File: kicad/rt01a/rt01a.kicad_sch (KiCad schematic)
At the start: 24 parts, among them J1 Barrel_Jack_Switch, J2 USB_C_Receptacle_USB2.0_14P, Q1 DMP3099L, U1 R-78E5.0-1.0, U2 MCP73831-2-OT, U3 TLV75533PDBV, U4 MCP111T-xxxE_TT

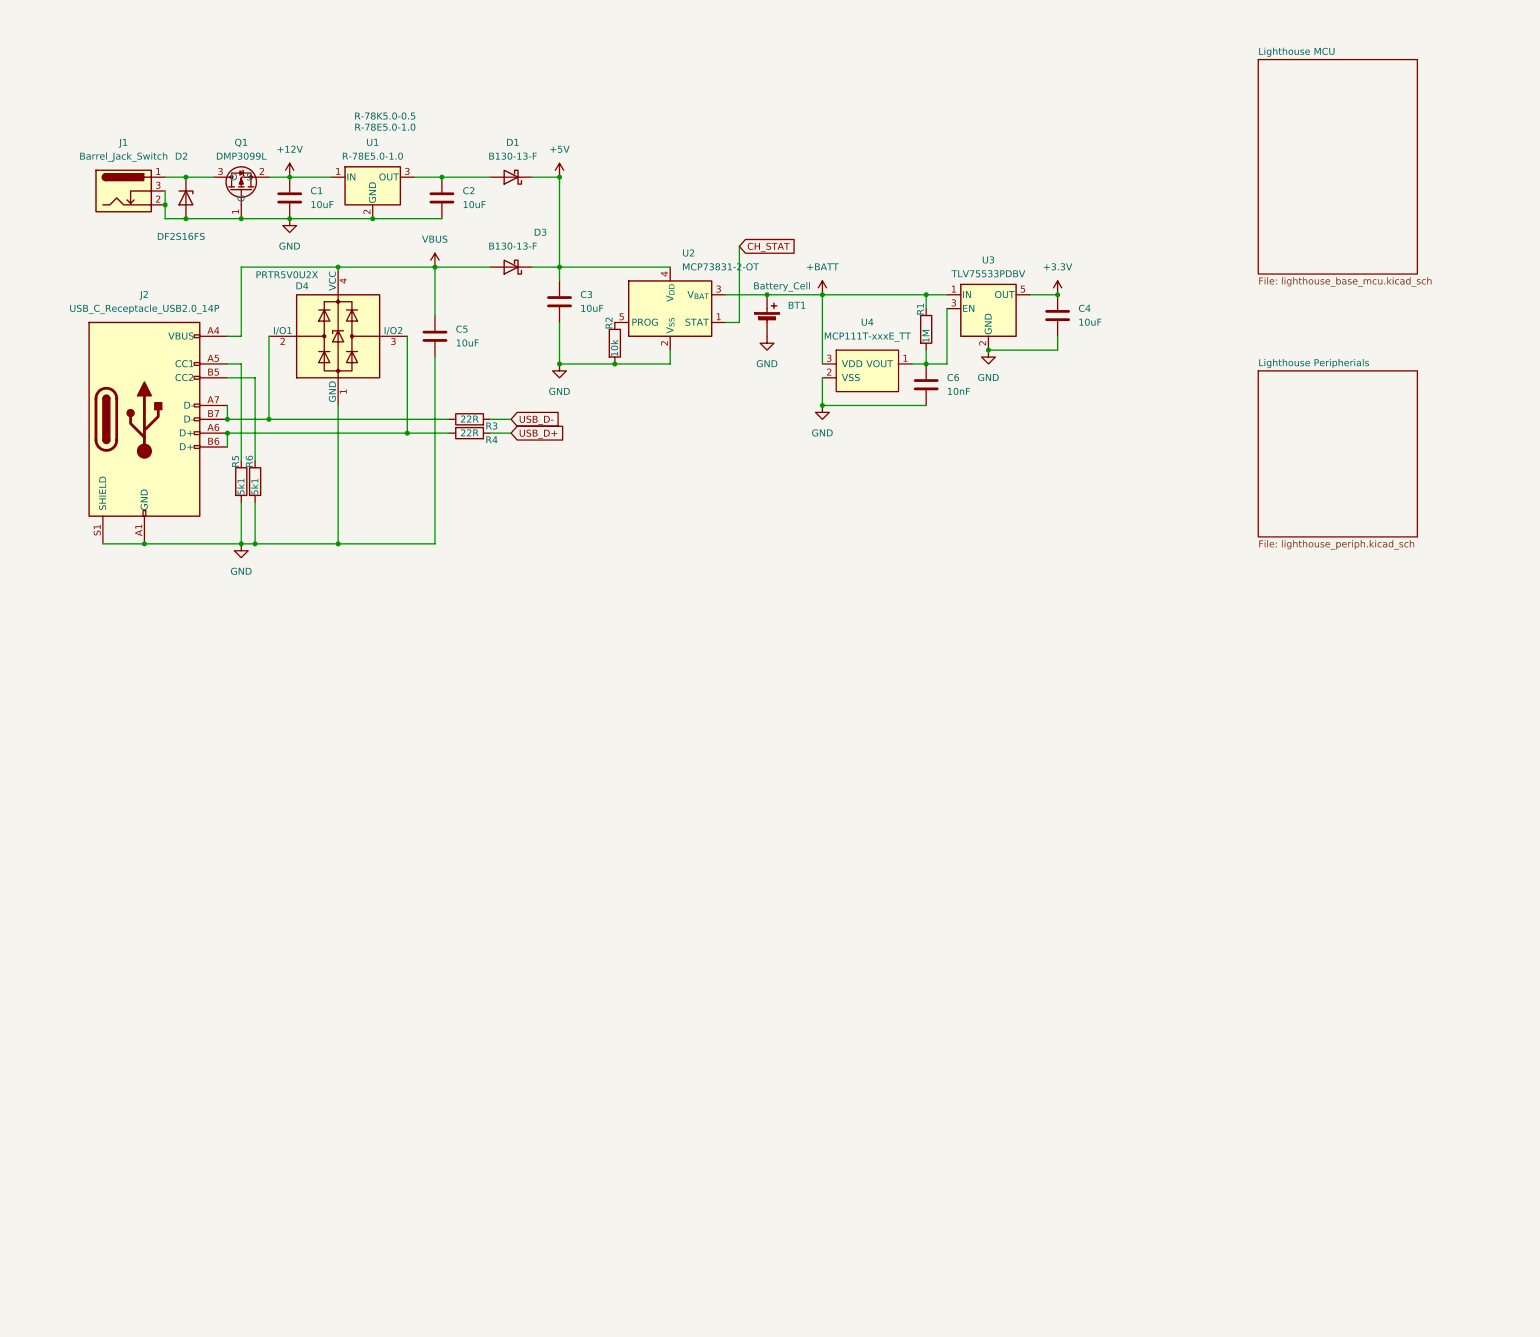
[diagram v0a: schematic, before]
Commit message: removed rt01a_1, _2, not needed anymore
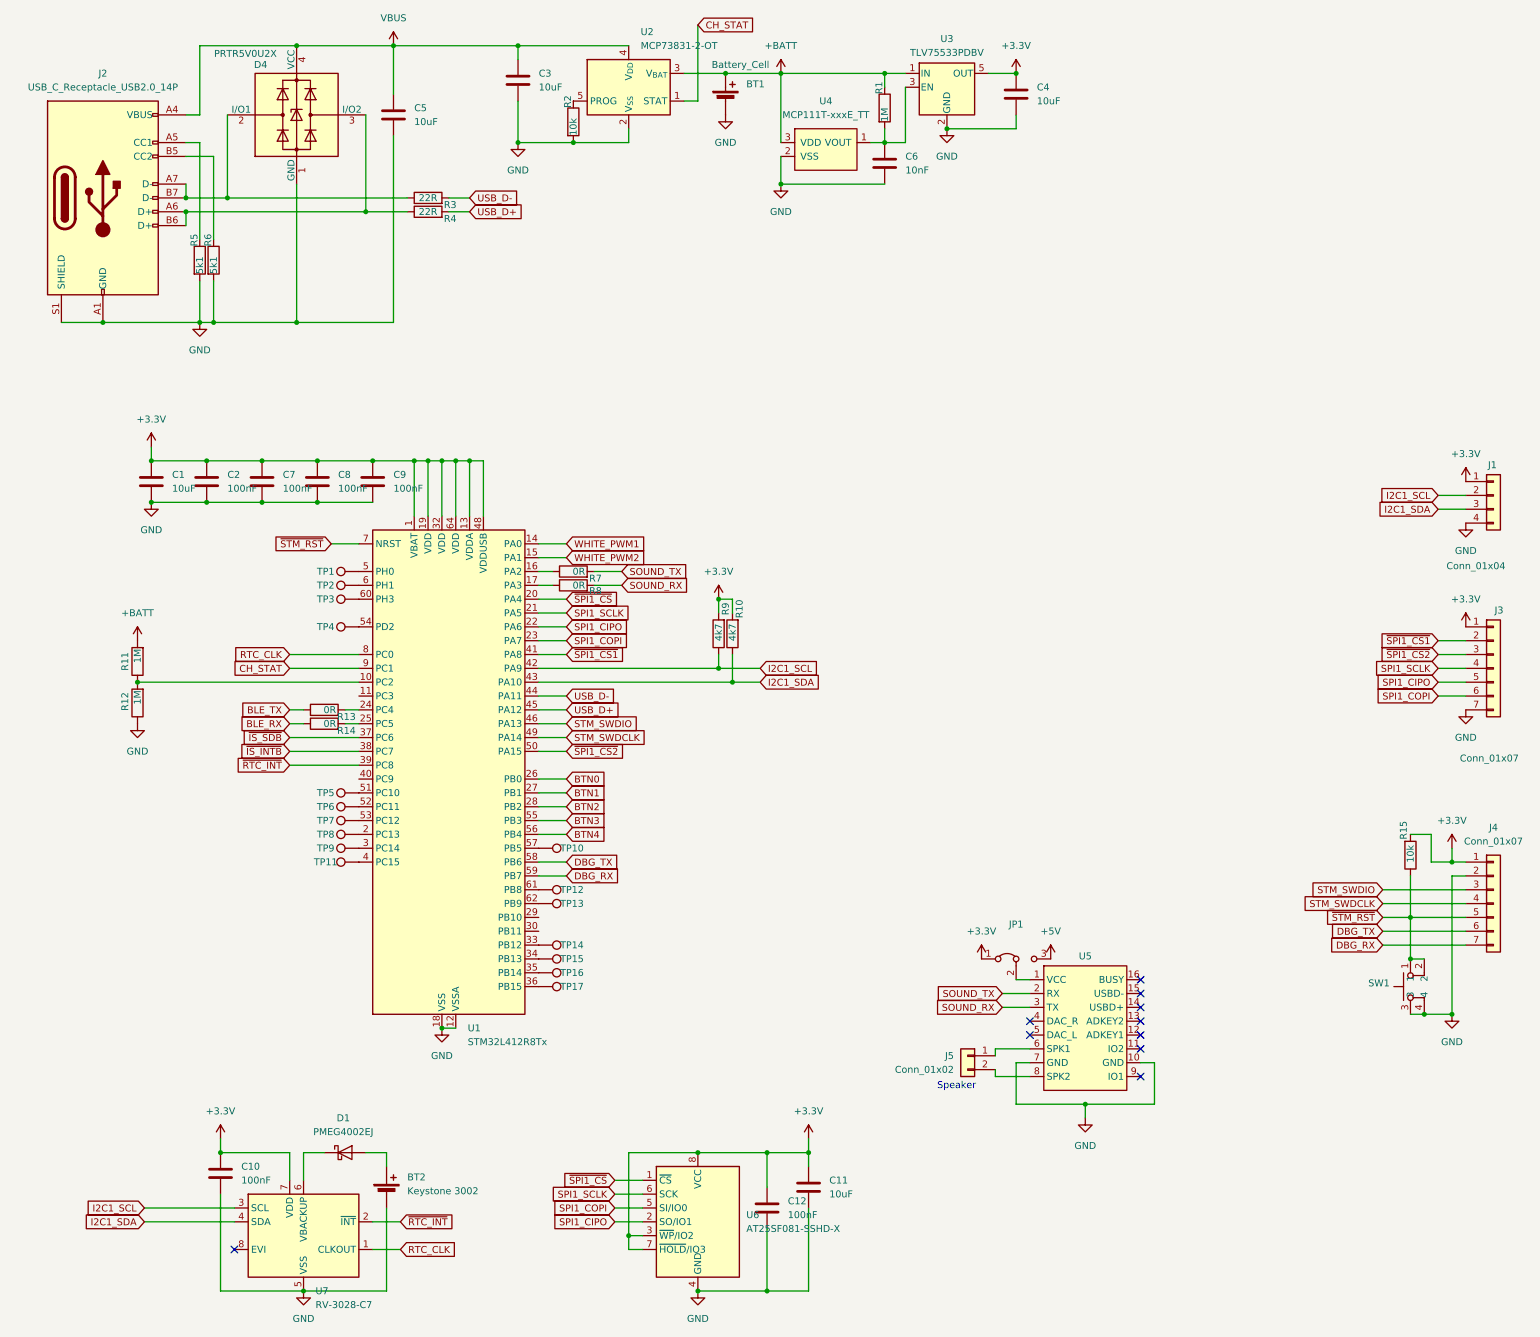
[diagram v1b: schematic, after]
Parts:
- removed D1, D3: B130-13-F, Diode_SMD:D_SMA_Handsoldering, symbol Device:D_Schottky
- removed D2: DF2S16FS, Diode_SMD:D_SOD-523, symbol Diode:ESD5Zxx
- removed J1: Barrel_Jack_Switch, Connector_BarrelJack:BarrelJack_CUI_PJ-063AH_Horizontal, symbol Connector:Barrel_Jack_Switch
- removed Q1: DMP3099L, Package_TO_SOT_SMD:SOT-23-3, symbol lighthouse1:DMP3099L_PMOSFET
- removed U1: R-78E5.0-1.0, Converter_DCDC:Converter_DCDC_RECOM_R-78E-0.5_THT, symbol Regulator_Switching:R-78E5.0-1.0
- added BT2: Keystone 3002, Battery:BatteryHolder_Keystone_3002_1x2032, symbol Device:Battery_Cell
- added C10, C12, C7, C8, C9: 100nF, Capacitor_SMD:C_0603_1608Metric_Pad1.08x0.95mm_HandSolder, symbol Device:C
- added C11: 10uF, Capacitor_SMD:C_0805_2012Metric_Pad1.18x1.45mm_HandSolder, symbol Device:C
- added D1: PMEG4002EJ, Diode_SMD:D_SOD-323F, symbol Diode:PMEG4002EJ
- added J1: Conn_01x04, Connector_PinHeader_2.54mm:PinHeader_1x04_P2.54mm_Vertical, symbol Connector_Generic:Conn_01x04
- added J3: Conn_01x07, Connector_PinHeader_2.54mm:PinHeader_1x07_P2.54mm_Vertical, symbol Connector_Generic:Conn_01x07
- added J4: Conn_01x07, Connector_PinHeader_1.27mm:PinHeader_1x07_P1.27mm_Vertical, symbol Connector_Generic:Conn_01x07
- added J5: Conn_01x02, Connector_PinHeader_2.54mm:PinHeader_1x02_P2.54mm_Vertical, symbol Connector_Generic:Conn_01x02
- added JP1: Jumper_3_Bridged12, Jumper:SolderJumper-3_P1.3mm_Bridged2Bar12_RoundedPad1.0x1.5mm, symbol Jumper:Jumper_3_Bridged12
- added R10, R9: 4k7, Resistor_SMD:R_0603_1608Metric_Pad0.98x0.95mm_HandSolder, symbol Device:R
- added R11, R12: 1M, Resistor_SMD:R_0603_1608Metric_Pad0.98x0.95mm_HandSolder, symbol Device:R
- added R13, R14, R7, R8: 0R, Resistor_SMD:R_0603_1608Metric_Pad0.98x0.95mm_HandSolder, symbol Device:R
- added R15: 10k, Resistor_SMD:R_0603_1608Metric_Pad0.98x0.95mm_HandSolder, symbol Device:R
- added SW1: ~, lighthouse:PTS526, symbol lighthouse1:SW_PTS5236
- added TP1, TP10, TP11, TP12, TP13, TP14, TP15, TP16, TP17, TP2, TP3, TP4, TP5, TP6, TP7, TP8, TP9: TestPoint, TestPoint:TestPoint_Pad_D1.0mm, symbol Connector:TestPoint
- added U1: STM32L412R8Tx, Package_QFP:LQFP-64_10x10mm_P0.5mm, symbol MCU_ST_STM32L4:STM32L412R8Tx
- added U5: ~, lighthouse:DFPlayer_Mini-TF-16P, symbol lighthouse1:DFPlayer_Mini
- added U6: AT25SF081-SSHD-X, Package_SO:SOIC-8_3.9x4.9mm_P1.27mm, symbol Memory_Flash:AT25SF081-SSHD-X
- added U7: RV-3028-C7, Package_SON:MicroCrystal_C7_SON-8_1.5x3.2mm_P0.9mm, symbol Timer_RTC:RV-3028-C7
- C2: value 10uF -> 100nF; footprint Capacitor_SMD:C_0805_2012Metric_Pad1.18x1.45mm_HandSolder -> Capacitor_SMD:C_0603_1608Metric_Pad1.08x0.95mm_HandSolder
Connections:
- net +12V is gone; now on net +3.3V: C1.1
- net +3.3V: now also C2.1, C10.1, C11.1, C12.1, C7.1, C8.1, C9.1, J1.1 (Pin_1), J3.1 (Pin_1), J4.1 (Pin_1), JP1.1 (A), R10.2, R15.2, R9.2, U1.1 (VBAT), U1.13 (VDDA), U1.19 (VDD), U1.32 (VDD), U1.48 (VDDUSB), U1.64 (VDD), U6.3 (~{WP}/IO2), U6.7 (~{HOLD}/IO3), U6.8 (VCC), U7.7 (VDD)
- net +5V: now also JP1.3 (B); no longer C3.1, U2.4 (V_{DD})
- net +BATT: now also R11.2
- net CH_STAT: now also U1.9 (PC1)
- net GND: now also BT2.2 (-), C10.2, C11.2, C12.2, C7.2, C8.2, C9.2, J1.4 (Pin_4), J3.7 (Pin_7), J4.2 (Pin_2), R12.1, SW1.3, SW1.4, U1.12 (VSSA), U1.18 (VSS), U1.31 (VSS), U1.47 (VSS), U1.63 (VSS), U5.10 (GND), U5.7 (GND), U6.4 (GND), U7.5 (VSS)
- net USB_D+: now also U1.45 (PA12)
- net USB_D-: now also U1.44 (PA11)
- net VBUS: now also C3.1, U2.4 (V_{DD})
- new net: JP1.2 (C), U5.1 (VCC)
- new net: TP11.1, U1.4 (PC15)
- new net: TP15.1, U1.34 (PB13)
- new net: TP10.1, U1.57 (PB5)
- new net: R13.2, U1.24 (PC4)
- new net: TP5.1, U1.51 (PC10)
- new net: TP2.1, U1.6 (PH1)
- new net: J5.1 (Pin_1), U5.6 (SPK1)
- new net: J5.2 (Pin_2), U5.8 (SPK2)
- new net: TP4.1, U1.54 (PD2)
- new net: TP13.1, U1.62 (PB9)
- new net: TP9.1, U1.3 (PC14)
- new net: TP16.1, U1.35 (PB14)
- new net: TP7.1, U1.53 (PC12)
- new net: D1.1 (K), U7.6 (VBACKUP)
- new net: BT2.1 (+), D1.2 (A)
- new net: R11.1, R12.2, U1.10 (PC2)
- new net: R14.2, U1.25 (PC5)
- new net: R8.1, U1.17 (PA3)
- new net: TP3.1, U1.60 (PH3)
- new net: TP17.1, U1.36 (PB15)
- new net: TP14.1, U1.33 (PB12)
- new net: R7.1, U1.16 (PA2)
- new net: TP8.1, U1.2 (PC13)
- new net: TP1.1, U1.5 (PH0)
- new net: TP6.1, U1.52 (PC11)
- new net: TP12.1, U1.61 (PB8)
- new net BLE_RX: R14.1
- new net BLE_TX: R13.1
- new net BTN0: U1.26 (PB0)
- new net BTN1: U1.27 (PB1)
- new net BTN2: U1.28 (PB2)
- new net BTN3: U1.55 (PB3)
- new net BTN4: U1.56 (PB4)
- new net DBG_RX: J4.7 (Pin_7), U1.59 (PB7)
- new net DBG_TX: J4.6 (Pin_6), U1.58 (PB6)
- new net I2C1_SCL: J1.2 (Pin_2), R9.1, U1.42 (PA9), U7.3 (SCL)
- new net I2C1_SDA: J1.3 (Pin_3), R10.1, U1.43 (PA10), U7.4 (SDA)
- new net RTC_CLK: U1.8 (PC0), U7.1 (CLKOUT)
- new net SOUND_RX: R8.2, U5.3 (TX)
- new net SOUND_TX: R7.2, U5.2 (RX)
- new net SPI1_CIPO: J3.5 (Pin_5), U1.22 (PA6), U6.2 (SO/IO1)
- new net SPI1_COPI: J3.6 (Pin_6), U1.23 (PA7), U6.5 (SI/IO0)
- new net SPI1_SCLK: J3.4 (Pin_4), U1.21 (PA5), U6.6 (SCK)
- new net STM_SWDCLK: J4.4 (Pin_4), U1.49 (PA14)
- new net STM_SWDIO: J4.3 (Pin_3), U1.46 (PA13)
- new net WHITE_PWM1: U1.14 (PA0)
- new net WHITE_PWM2: U1.15 (PA1)
- new net ~{IS_INTB}: U1.38 (PC7)
- new net ~{IS_SDB}: U1.37 (PC6)
- new net ~{RTC_INT}: U1.39 (PC8), U7.2 (~{INT})
- new net ~{SPI1_CS1}: J3.2 (Pin_2), U1.41 (PA8)
- new net ~{SPI1_CS2}: J3.3 (Pin_3), U1.50 (PA15)
- new net ~{SPI1_CS}: U1.20 (PA4), U6.1 (~{CS})
- new net ~{STM_RST}: J4.5 (Pin_5), R15.1, SW1.1, SW1.2, U1.7 (NRST)
- no-connect marks 0 -> 10
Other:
- removed sheet Lighthouse MCU
- removed sheet Lighthouse Peripherials
- note added: "Speaker"
- note removed: "R-78K5.0-0.5 R-78E5.0-1.0"
- title: (none) -> round timer 1
- moved on the sheet: BT1, C3, C4, C5, C6, D4, J2, R1, R2, R3, R4, R5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

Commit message: rt01a added footprint, some placements done
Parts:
- removed BT2: Keystone 3002, Battery:BatteryHolder_Keystone_3002_1x2032, symbol Device:Battery_Cell
- removed D1: PMEG4002EJ, Diode_SMD:D_SOD-323F, symbol Diode:PMEG4002EJ
- removed J1: Conn_01x04, Connector_PinHeader_2.54mm:PinHeader_1x04_P2.54mm_Vertical, symbol Connector_Generic:Conn_01x04
- removed J3: Conn_01x07, Connector_PinHeader_2.54mm:PinHeader_1x07_P2.54mm_Vertical, symbol Connector_Generic:Conn_01x07
- added R16: 10k, Resistor_SMD:R_0603_1608Metric_Pad0.98x0.95mm_HandSolder, symbol Device:R
- added TP18, TP19, TP20, TP21: TestPoint, TestPoint:TestPoint_Pad_D1.0mm, symbol Connector:TestPoint
- C3: value 10uF -> 10nF; footprint Capacitor_SMD:C_0805_2012Metric_Pad1.18x1.45mm_HandSolder -> Capacitor_SMD:C_0603_1608Metric_Pad1.08x0.95mm_HandSolder
- SW1: value ~ -> EVPBT3G4A000; footprint lighthouse:PTS526 -> rt:EVPBT3
- U5: footprint lighthouse:DFPlayer_Mini-TF-16P -> rt:DFPlayer_Mini-TF-16P
- renumbered C5 to C1, C4 to C2, C6 to C4, C1 to C5, C2 to C6, D4 to D1, J2 to J1, U2 to U1, U3 to U2, U4 to U3, U1 to U4
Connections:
- net +3.3V: now also TP18.1
- net GND: now also R16.1, TP21.1
- net I2C1_SCL: now also TP19.1
- net I2C1_SDA: now also TP20.1
- net VBUS: no longer C3.1
- net ~{STM_RST}: now also C3.1
- net at U7.6 (VBACKUP): now also R16.2
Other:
- moved on the sheet: BT1, C1, C2, C4, D1, J1, R1, R2, R3, R4, R5, R6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

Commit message: schematics seems done
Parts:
- removed J5: Conn_01x02, Connector_PinHeader_2.54mm:PinHeader_1x02_P2.54mm_Vertical, symbol Connector_Generic:Conn_01x02
- removed JP1: Jumper_3_Bridged12, Jumper:SolderJumper-3_P1.3mm_Bridged2Bar12_RoundedPad1.0x1.5mm, symbol Jumper:Jumper_3_Bridged12
- removed R13: 0R, Resistor_SMD:R_0603_1608Metric_Pad0.98x0.95mm_HandSolder, symbol Device:R
- removed TP17, TP18, TP19, TP20, TP21: TestPoint, TestPoint:TestPoint_Pad_D1.0mm, symbol Connector:TestPoint
- added C13, C22: 10uF, Capacitor_SMD:C_0805_2012Metric_Pad1.18x1.45mm_HandSolder, symbol Device:C
- added C14, C20, C21, C23: 100nF, Capacitor_SMD:C_0603_1608Metric_Pad1.08x0.95mm_HandSolder, symbol Device:C
- added C15, C16, C17, C18, C19: 10nF, Capacitor_SMD:C_0603_1608Metric_Pad1.08x0.95mm_HandSolder, symbol Device:C
- added D2: D_Schottky, Diode_SMD:D_SOD-523, symbol Device:D_Schottky
- added D3, D4, D5, D6, D7, D8: ESD5Zxx, Diode_SMD:D_SMF, symbol Diode:ESD5Zxx
- added Q1, Q2: Q_NMOS_DGS, Package_TO_SOT_SMD:SOT-23-3, symbol Device:Q_NMOS_DGS
- added R15: 10R, Resistor_SMD:R_0603_1608Metric_Pad0.98x0.95mm_HandSolder, symbol Device:R
- added R17: 1M, Resistor_SMD:R_0603_1608Metric_Pad0.98x0.95mm_HandSolder, symbol Device:R
- added R18, R19, R20, R21, R22, R23, R24, R25, R26, R27, R28, R29: 10k, Resistor_SMD:R_0603_1608Metric_Pad0.98x0.95mm_HandSolder, symbol Device:R
- added U10: LTR-303ALS-01, OptoDevice:Lite-On_LTR-303ALS-01, symbol Sensor_Optical:LTR-303ALS-01
- added U11: LSM303C, Package_LGA:LGA-12_2x2mm_P0.5mm, symbol Sensor_Motion:LSM303C
- added U8: GC9A01, rt:FP-128HR01A, symbol rt:GC9A01
- added U9: SHTC3, Sensor_Humidity:Sensirion_DFN-4-1EP_2x2mm_P1mm_EP0.7x1.6mm, symbol Sensor_Humidity:SHTC3
- R14: value 0R -> 1M
- U7: renamed from U5; footprint rt:DFPlayer_Mini-TF-16P -> rt:DFPlayer_Mini-TF-16P_Minimal; symbol lighthouse1:DFPlayer_Mini -> rt:DFPlayer_Mini_Minimal
- renumbered C5 to C1, C4 to C10, C2 to C11, C3 to C12, C6 to C2, C10 to C3, C7 to C4, C8 to C5, C9 to C6, C1 to C7, C12 to C8, C11 to C9, J4 to J2, R11 to R1, R2 to R10, R9 to R11, R10 to R12, R1 to R13, R15 to R16, R12 to R2, R5 to R3, R6 to R4, R16 to R5, R3 to R6, R4 to R7, R7 to R8, R8 to R9, U7 to U1, U4 to U2, U1 to U3, U6 to U4, U3 to U5, U2 to U6
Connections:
- net BTN4 is gone; now on net BTN3: U2.56 (PB4)
- net WHITE_PWM1 is gone; now on net RTC_CLK: U2.14 (PA0)
- net ~{IS_SDB} is gone; now on net CH_STAT: U2.37 (PC6)
- net +3.3V: now also TP1.1, TP14.1, U7.1 (VCC), C13.1, C14.1, C20.1, C21.1, C22.1, C23.1, D2.1 (K), R23.2, R24.2, R25.2, R26.2, R27.2, U10.1 (VDD), U11.10 (VDDIO), U11.9 (VDD), U8.3 (LEDA), U8.4 (VDD), U9.1 (VDD)
- net BTN1: now also U2.28 (PB2), R20.1; no longer U2.27 (PB1)
- net BTN2: now also U2.55 (PB3), R21.1; no longer U2.28 (PB2)
- net BTN3: now also R22.1; no longer U2.55 (PB3)
- net CH_STAT: no longer U2.9 (PC1)
- net DBG_RX: now also U2.8 (PC0); no longer U2.59 (PB7)
- net DBG_TX: now also U2.9 (PC1); no longer U2.58 (PB6)
- net GND: now also R14.2, TP11.1, TP13.1, TP2.1, TP7.1, TP9.1, C13.2, C14.2, C15.2, C16.2, C17.2, C18.2, C19.2, C20.2, C21.2, C22.2, C23.2, D3.2 (A), D4.2 (A), D5.2 (A), D6.2 (A), D7.2 (A), D8.2 (A), Q1.3 (S), Q2.3 (S), R17.2, U10.3 (GND), U11.6 (GND), U11.8 (GND), U8.1 (GND), U8.12 (GND), U8.5 (GND), U8.6 (GND), U9.4 (VSS)
- net I2C1_SCL: now also TP3.1, U10.6 (SDA), U11.1 (SCL/SPC), U9.2 (SCL)
- net I2C1_SDA: now also TP4.1, U10.4 (SCL), U11.4 (SDA/SDI/SDO), U9.3 (SDA)
- net RTC_CLK: no longer U2.8 (PC0)
- net at U2.4 (PC15): no longer TP11.1
- net at TP15.1: now also D2.2 (A), D8.1 (K), Q2.1 (D); no longer U2.34 (PB13)
- net at TP10.1: now also C18.1, D6.1 (K), R21.2, R26.1; no longer U2.57 (PB5)
- net at TP5.1: now also C15.1, D3.1 (K), R18.2, R23.1, R28.2; no longer U2.51 (PC10)
- net at U2.6 (PH1): no longer TP2.1
- net at U2.54 (PD2): no longer TP4.1
- net at U2.62 (PB9): no longer TP13.1
- net at U2.3 (PC14): no longer TP9.1
- net at TP16.1: now also U2.36 (PB15); no longer U2.35 (PB14)
- net at U2.53 (PC12): no longer TP7.1
- net at U2.25 (PC5): no longer R14.2
- net at U2.60 (PH3): no longer TP3.1
- net DISP_CS: now reaches U2.33 (PB12)
- net DISP_CS: now also U8.8 (CS); no longer TP14.1
- net at TP8.1: now also C17.1, D7.1 (K), R20.2, R25.1; no longer U2.2 (PC13)
- net DISP_RST: now reaches U2.29 (PB10)
- net DISP_RST: now also U8.11 (RESET)
- net DISP_DC: now reaches U2.30 (PB11)
- net DISP_DC: now also U8.7 (D/C)
- net at U2.5 (PH0): no longer TP1.1
- net at TP6.1: now also C16.1, D4.1 (K), R19.2, R24.1, R29.2; no longer U2.52 (PC11)
- net at TP12.1: now also C19.1, D5.1 (K), R22.2, R27.1; no longer U2.61 (PB8)
- net BLE_RX renamed DISP_BG
- net DISP_BG: now also U2.61 (PB8), Q1.2 (G)
- net BTN0 renamed ROT_A
- net ROT_A: now also R28.1
- net WHITE_PWM2: no longer names the net of U2.15 (PA1)
- net ~{IS_INTB} renamed RTC_INT
- net RTC_INT: now also U1.2 (~{INT})
- net ~{RTC_INT}: no longer names the net of U2.39 (PC8)
- net ~{RTC_INT}: no longer U1.2 (~{INT})
- new net: Q1.1 (D), R15.2
- new net: R15.1, U8.2 (LEDK)
- new net DISP_MOSI: U2.35 (PB14), U8.10 (SDA)
- new net DISP_SCK: U2.34 (PB13), U8.9 (SCL)
- new net ROT_A1: R18.1, U2.57 (PB5)
- new net ROT_B: R19.1, U2.27 (PB1)
- new net ROT_B1: R29.1, U2.59 (PB7)
- new net VIBRA: Q2.2 (G), R17.1, U2.58 (PB6)
- no-connect marks 10 -> 2
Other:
- note added: "ACC/Mag"
- note added: "BTN EVPBT3G4A000"
- note added: "BTN Rotary Encoder"
- note added: "L"
- note added: "RH"
- note added: "RTC"
- note added: "Rotary Encoder"
- note added: "Vibra Motor"
- note added: "connect Speaker directly to SPK1 SPK2"
- note added: "in out"
- note removed: "Speaker"
- moved on the sheet: C12, C3, C8, C9, J2, R16, R5, SW1, U1, U4
